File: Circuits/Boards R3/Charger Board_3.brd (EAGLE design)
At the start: 97.2 x 69.8 mm, 117 parts, among them CON1 ISP(2X3), CON13 HEADER_4X1, CON14 HEADER_3X1, CON15 HEADER_3X1, CON16 HEADER_4X1, CON17 HEADER_3X1, CON18 HEADER_3X1, CON19 HEADER_4X1, CON2 SCREWTERMINAL_1X2, CON20 HEADER_4X1, CON21 HEADER_4X1, CON22 HEADER_4X1, CON23 HEADER_4X1, CON24 HEADER_4X1, CON25 HEADER_4X1, CON26 HEADER_4X1, CON27 HEADER_4X1, CON28 HEADER_4X1, T1 IRLML6244TR, T2 IRLML6244TR, T3 SI4421DY, T4 IRLML6244TR, T5 IRLML6244TR, T6 IRLML6244TR, T7 IRLML6244TR, U1 ATMEGA324P, U2 ACS711, U3 JOYSTICKPTH, U4 MX25L25735E, U5 ATMEGA1281

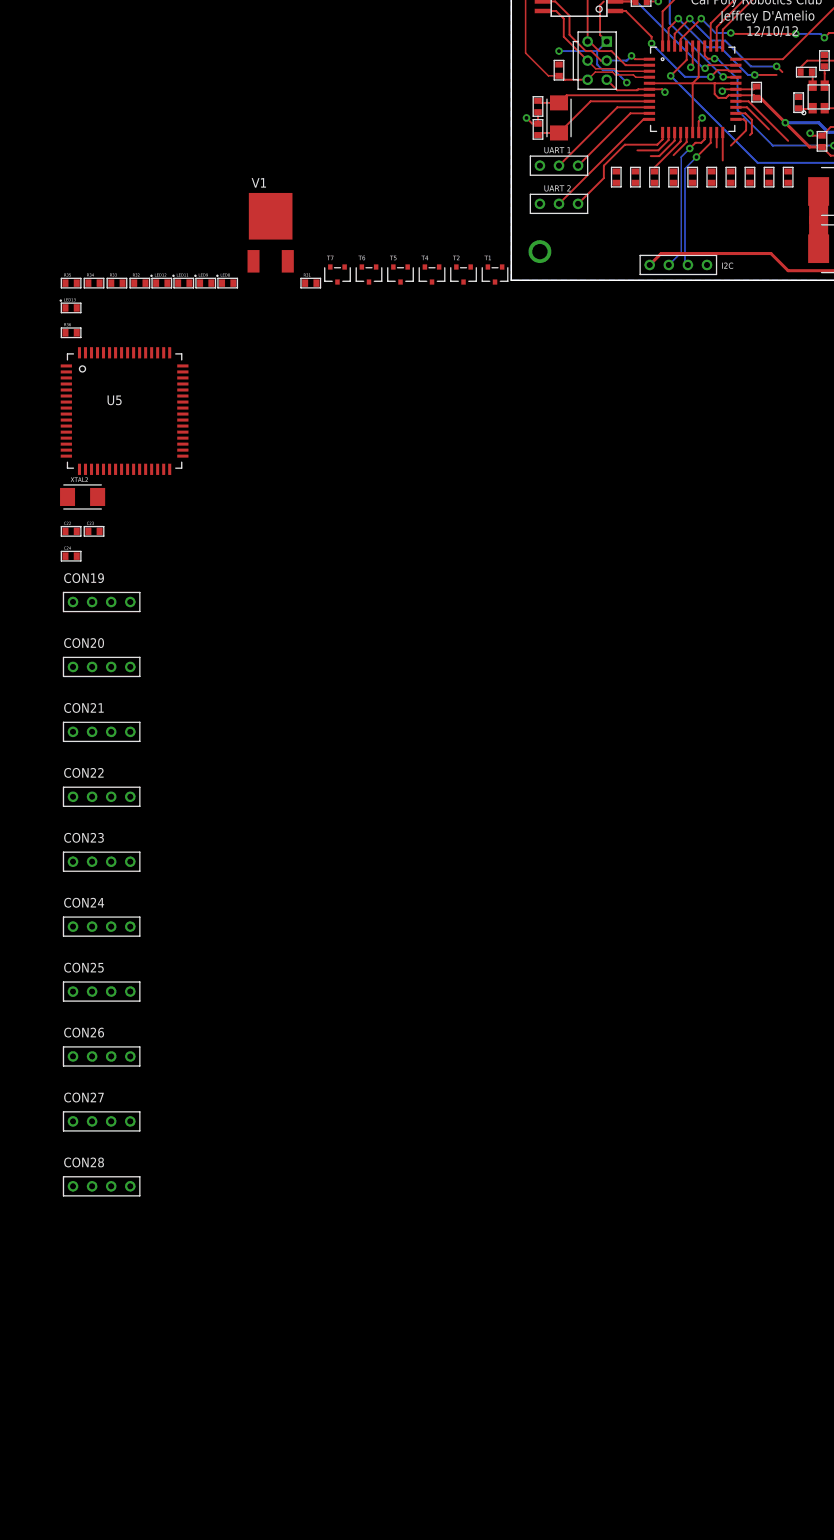
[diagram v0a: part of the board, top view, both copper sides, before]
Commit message: Both boards almost ready for routing
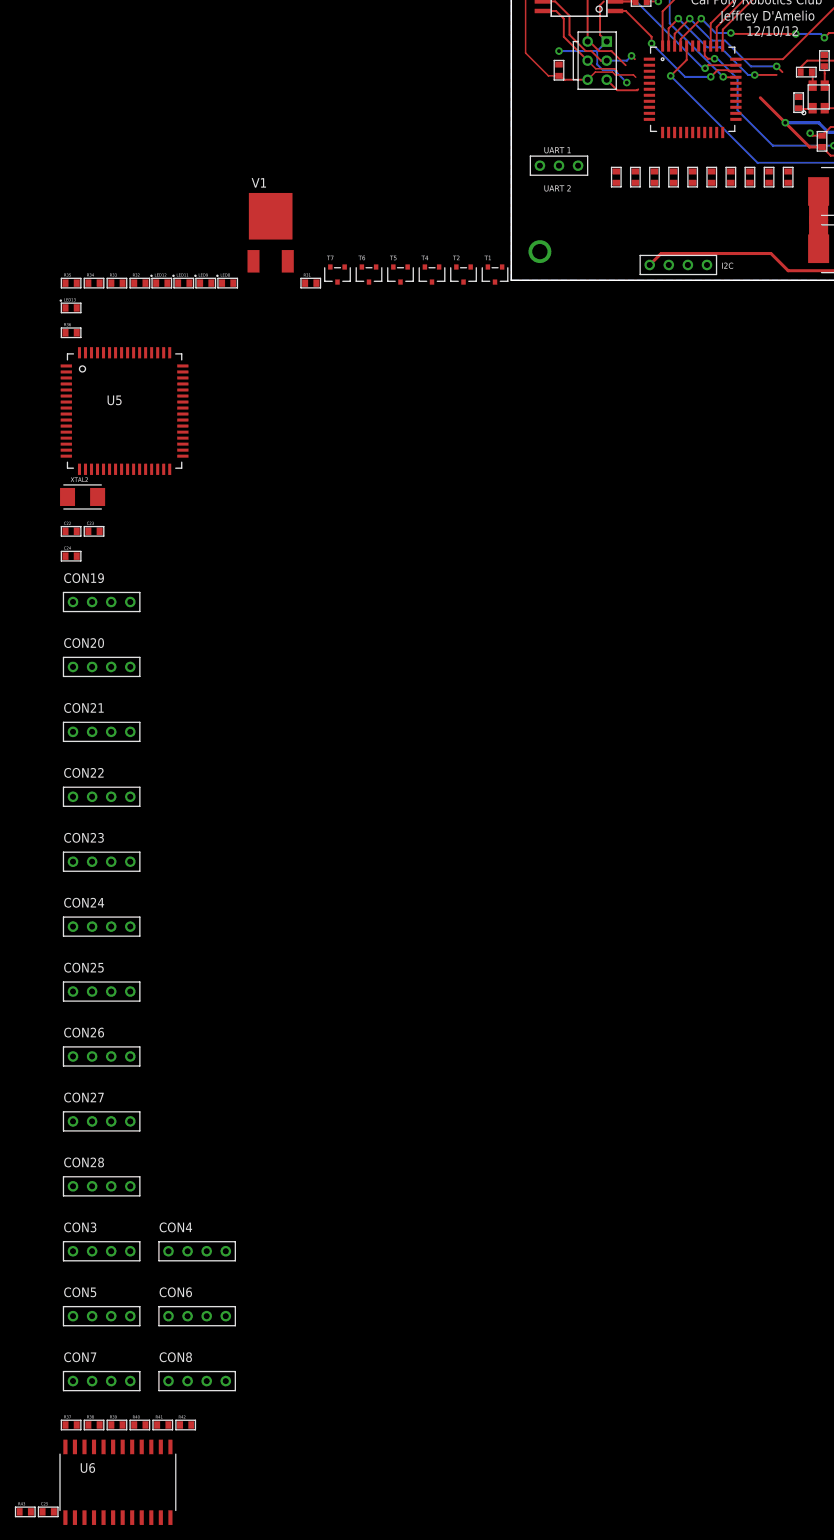
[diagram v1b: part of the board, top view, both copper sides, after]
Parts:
- removed C10, C11: 12pf, Passive:0603
- removed C3: 1uf, Passive:0603
- removed CON18: HEADER_3X1, Mechanical:3PINHEADER_.100"
- removed XTAL1: 10Mhz, Passive:SMDXTAL
- added C25: 1uf, Passive:0603
- added CON3, CON4, CON5, CON6, CON7, CON8: HEADER_4X1, Mechanical:4PINHEADER_.100"
- added R37, R38, R39, R40, R41, R42: 300, Passive:0603
- added R43: 10k, Passive:0603
- added U6: CD74HC154M96, DigitalIC:24SOIC
- C24: value 1uf -> .1uf
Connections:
- removed net N$12: C10.1, U1.7, XTAL1.2
- removed net N$18: C14.2, S1.1, S1.2
- removed net N$19: CON18.3, U1.12
- removed net N$25: C11.1, U1.8, XTAL1.1
- removed net N$4: CON18.2, U1.11
- removed net N$7: CON17.3, U1.10
- removed net N$8: CON17.2, U1.9
- removed net SCL: CON13.2, U1.19
- removed net SDA: CON13.3, U1.20
- removed net SECTION1: U1.13
- removed net SECTION10: U1.26
- removed net SECTION2: U1.14
- removed net SECTION3: U1.15
- removed net SECTION4: U1.16
- removed net SECTION5: U1.21
- removed net SECTION6: U1.22
- removed net SECTION7: U1.23
- removed net SECTION8: U1.24
- removed net SECTION9: U1.25
- new net A0: U6.P$23
- new net A1: U6.P$22
- new net A2: U6.P$21
- new net A3: U6.P$20
- new net CTX: U5.P$3, U6.P$18
- new net CTX11: CON3.3, U6.P$11
- new net CTX12: CON4.3, U6.P$13
- new net CTX13: CON5.3, U6.P$14
- new net CTX14: CON6.3, U6.P$15
- new net CTX15: CON7.3, U6.P$16
- new net CTX16: CON8.3, U6.P$17
- new net N$49: CON3.4, R37.2
- new net N$50: CON4.4, R38.2
- new net N$51: CON5.4, R39.2
- new net N$52: CON6.4, R40.2
- new net N$53: CON7.4, R41.2
- new net N$54: CON8.4, R42.2
- new net N$55: CON13.2, U5.P$25
- new net N$56: CON13.3, U5.P$26
- new net N$57: R43.1, U6.P$19
- new net N$60: CON17.2, U5.P$27
- new net N$61: CON17.3, U5.P$28
- net +3V: now also C25.1, U6.P$24; no longer C3.1, U1.17, U1.27, U1.29, U1.38, U1.5
- net CHARGE+: now also CON3.2, CON4.2, CON5.2, CON6.2, CON7.2, CON8.2
- net CRX: now also R37.1, R38.1, R39.1, R40.1, R41.1, R42.1, U5.P$2
- net CTX1: now also U6.P$1
- net CTX10: now also U6.P$10
- net CTX2: now also U6.P$2
- net CTX3: now also U6.P$3
- net CTX4: now also U6.P$4
- net CTX5: now also U6.P$5
- net CTX6: now also U6.P$6
- net CTX7: now also U6.P$7
- net CTX8: now also U6.P$8
- net CTX9: now also U6.P$9
- net GND: now also C14.2, C25.2, CON3.1, CON4.1, CON5.1, CON6.1, CON7.1, CON8.1, R43.2, S1.1, S1.2, U6.P$12; no longer C10.2, C11.2, C3.2, CON18.1, U1.18, U1.28, U1.39, U1.6
- net MISO: no longer U1.2
- net MOSI: no longer U1.1
- net RESET: no longer U1.4
- net SCK: no longer U1.3
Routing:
- net +3V: track 205.6 -> 174.7 mm
- net SCL: track 20.0 -> 0.00 mm, vias 1 -> 0
- net SDA: track 19.2 -> 0.00 mm, vias 1 -> 0
- net N$4: track 16.7 -> 0.00 mm
- net N$19: track 16.7 -> 0.00 mm
- net N$25: track 16.6 -> 0.00 mm
- net N$12: track 15.3 -> 0.00 mm
- net N$8: track 15.2 -> 0.00 mm
- net GND: track 54.2 -> 40.5 mm, vias 10 -> 5
- net N$7: track 12.4 -> 0.00 mm
- net SECTION10: track 9.13 -> 0.00 mm
- net SECTION3: track 6.11 -> 0.00 mm
- net SECTION1: track 5.73 -> 0.00 mm
- net SECTION9: track 5.63 -> 0.00 mm
- net SECTION7: track 5.51 -> 0.00 mm
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
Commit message: same as last
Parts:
- added TST1, TST2: TESTPOINT, Mechanical:TESTPOINT
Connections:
- new net DEBUG1: TST2.P$1
- new net DEBUG2: TST1.P$1
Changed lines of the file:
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@@
 <setting verticaltext="up"/>
 </settings>
-<grid distance="0.005" unitdist="inch" unit="mm" style="lines" multiple="1" display="no" altdistance="0.005" altunitdist="inch" altunit="inch"/>
+<grid distance="0.005" unitdist="inch" unit="inch" style="lines" multiple="1" display="no" altdistance="0.005" altunitdist="inch" altunit="inch"/>
 <layers>
 <layer number="1" name="Top" color="4" fill="1" visible="yes" active="yes"/>
@@
 <element name="C25" library="Passive" package="0603" value="1uf" x="-61.595" y="-163.83"/>
 <element name="R43" library="Passive" package="0603" value="10k" x="-64.643" y="-163.83"/>
+<element name="TST1" library="Mechanical" package="TESTPOINT" value="TESTPOINT" x="-65.151" y="-166.878"/>
+<element name="TST2" library="Mechanical" package="TESTPOINT" value="TESTPOINT" x="-65.151" y="-169.799"/>
 </elements>
 <signals>
@@
 <wire x1="8.89" y1="15.24" x2="-48.635" y2="-25.149" width="0" layer="19" extent="1-1"/>
 </signal>
+<signal name="DEBUG1">
+<contactref element="TST2" pad="P$1"/>
+</signal>
+<signal name="DEBUG2">
+<contactref element="TST1" pad="P$1"/>
+</signal>
 </signals>
